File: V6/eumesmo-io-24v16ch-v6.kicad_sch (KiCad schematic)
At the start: 9 parts, among them J1 250-208, J2 250-208, J3 250-208, J4 250-208, J5 250-202

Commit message: Renamed all files to eumesmo branding
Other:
- sheet I2C Devices: file esp-24v-16ch-v6-i2c.kicad_sch -> eumesmo-io-24v16ch-v6-i2c.kicad_sch
- sheet Input 1: file esp-24v-16ch-v6-inputs1-8.kicad_sch -> eumesmo-io-24v16ch-v6-inputs1-8.kicad_sch
- sheet Input 10: file esp-24v-16ch-v6-inputs9-16.kicad_sch -> eumesmo-io-24v16ch-v6-inputs9-16.kicad_sch
- sheet Input 11: file esp-24v-16ch-v6-inputs9-16.kicad_sch -> eumesmo-io-24v16ch-v6-inputs9-16.kicad_sch
- sheet Input 12: file esp-24v-16ch-v6-inputs9-16.kicad_sch -> eumesmo-io-24v16ch-v6-inputs9-16.kicad_sch
- sheet Input 13: file esp-24v-16ch-v6-inputs9-16.kicad_sch -> eumesmo-io-24v16ch-v6-inputs9-16.kicad_sch
- sheet Input 14: file esp-24v-16ch-v6-inputs9-16.kicad_sch -> eumesmo-io-24v16ch-v6-inputs9-16.kicad_sch
- sheet Input 15: file esp-24v-16ch-v6-inputs9-16.kicad_sch -> eumesmo-io-24v16ch-v6-inputs9-16.kicad_sch
- sheet Input 16: file esp-24v-16ch-v6-inputs9-16.kicad_sch -> eumesmo-io-24v16ch-v6-inputs9-16.kicad_sch
- sheet Input 2: file esp-24v-16ch-v6-inputs1-8.kicad_sch -> eumesmo-io-24v16ch-v6-inputs1-8.kicad_sch
- sheet Input 3: file esp-24v-16ch-v6-inputs1-8.kicad_sch -> eumesmo-io-24v16ch-v6-inputs1-8.kicad_sch
- sheet Input 4: file esp-24v-16ch-v6-inputs1-8.kicad_sch -> eumesmo-io-24v16ch-v6-inputs1-8.kicad_sch
- sheet Input 5: file esp-24v-16ch-v6-inputs1-8.kicad_sch -> eumesmo-io-24v16ch-v6-inputs1-8.kicad_sch
- sheet Input 6: file esp-24v-16ch-v6-inputs1-8.kicad_sch -> eumesmo-io-24v16ch-v6-inputs1-8.kicad_sch
- sheet Input 7: file esp-24v-16ch-v6-inputs1-8.kicad_sch -> eumesmo-io-24v16ch-v6-inputs1-8.kicad_sch
- sheet Input 8: file esp-24v-16ch-v6-inputs1-8.kicad_sch -> eumesmo-io-24v16ch-v6-inputs1-8.kicad_sch
- sheet Input 9: file esp-24v-16ch-v6-inputs9-16.kicad_sch -> eumesmo-io-24v16ch-v6-inputs9-16.kicad_sch
- sheet LAN: file esp-24v-16ch-v6-lan.kicad_sch -> eumesmo-io-24v16ch-v6-lan.kicad_sch
- sheet MCU: file esp-24v-16ch-v6-mcu.kicad_sch -> eumesmo-io-24v16ch-v6-mcu.kicad_sch
- sheet Output 1: file esp-24v-16ch-v6-outputs1-8.kicad_sch -> eumesmo-io-24v16ch-v6-outputs1-8.kicad_sch
- sheet Output 10: file esp-24v-16ch-v6-outputs9-16.kicad_sch -> eumesmo-io-24v16ch-v6-outputs9-16.kicad_sch
- sheet Output 11: file esp-24v-16ch-v6-outputs9-16.kicad_sch -> eumesmo-io-24v16ch-v6-outputs9-16.kicad_sch
- sheet Output 12: file esp-24v-16ch-v6-outputs9-16.kicad_sch -> eumesmo-io-24v16ch-v6-outputs9-16.kicad_sch
- sheet Output 13: file esp-24v-16ch-v6-outputs9-16.kicad_sch -> eumesmo-io-24v16ch-v6-outputs9-16.kicad_sch
- sheet Output 14: file esp-24v-16ch-v6-outputs9-16.kicad_sch -> eumesmo-io-24v16ch-v6-outputs9-16.kicad_sch
- sheet Output 15: file esp-24v-16ch-v6-outputs9-16.kicad_sch -> eumesmo-io-24v16ch-v6-outputs9-16.kicad_sch
- sheet Output 16: file esp-24v-16ch-v6-outputs9-16.kicad_sch -> eumesmo-io-24v16ch-v6-outputs9-16.kicad_sch
- sheet Output 2: file esp-24v-16ch-v6-outputs1-8.kicad_sch -> eumesmo-io-24v16ch-v6-outputs1-8.kicad_sch
- sheet Output 3: file esp-24v-16ch-v6-outputs1-8.kicad_sch -> eumesmo-io-24v16ch-v6-outputs1-8.kicad_sch
- sheet Output 4: file esp-24v-16ch-v6-outputs1-8.kicad_sch -> eumesmo-io-24v16ch-v6-outputs1-8.kicad_sch
- sheet Output 5: file esp-24v-16ch-v6-outputs1-8.kicad_sch -> eumesmo-io-24v16ch-v6-outputs1-8.kicad_sch
- sheet Output 6: file esp-24v-16ch-v6-outputs1-8.kicad_sch -> eumesmo-io-24v16ch-v6-outputs1-8.kicad_sch
- sheet Output 7: file esp-24v-16ch-v6-outputs1-8.kicad_sch -> eumesmo-io-24v16ch-v6-outputs1-8.kicad_sch
- sheet Output 8: file esp-24v-16ch-v6-outputs1-8.kicad_sch -> eumesmo-io-24v16ch-v6-outputs1-8.kicad_sch
- sheet Output 9: file esp-24v-16ch-v6-outputs9-16.kicad_sch -> eumesmo-io-24v16ch-v6-outputs9-16.kicad_sch
- sheet Power: file esp-24v-16ch-v6-power.kicad_sch -> eumesmo-io-24v16ch-v6-power.kicad_sch
- title: ESP 24V 16xIn/16xOut/1-Wire Module -> eumesmo 24V 16xIn/16xOut/1-Wire Module

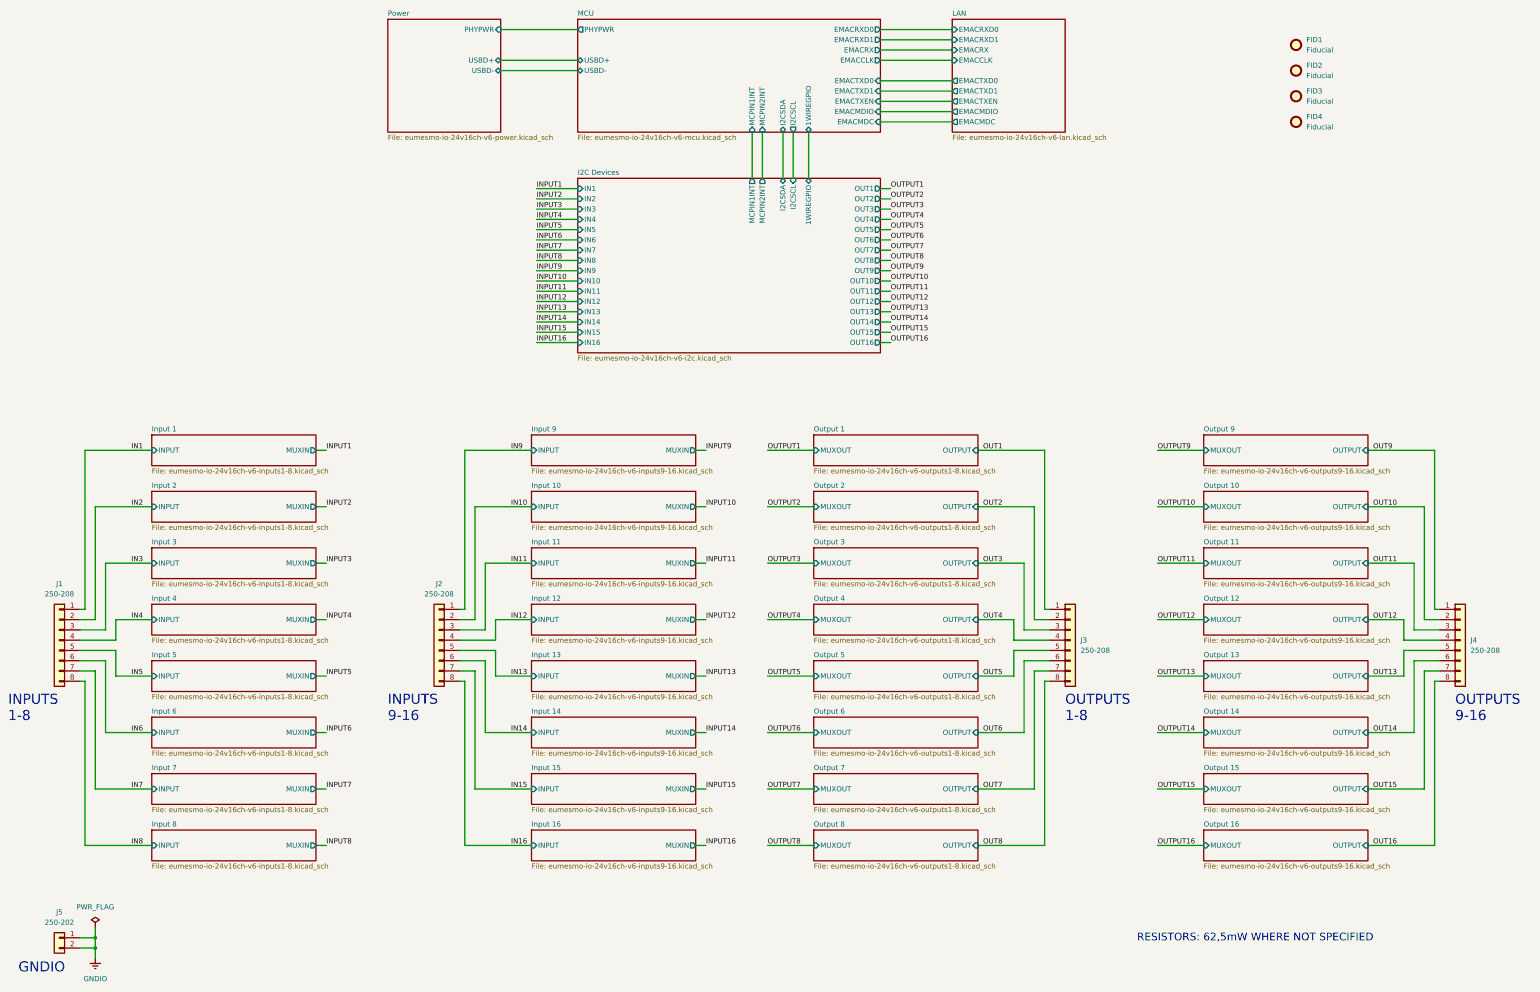
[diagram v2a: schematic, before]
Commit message: Added CPU health LED
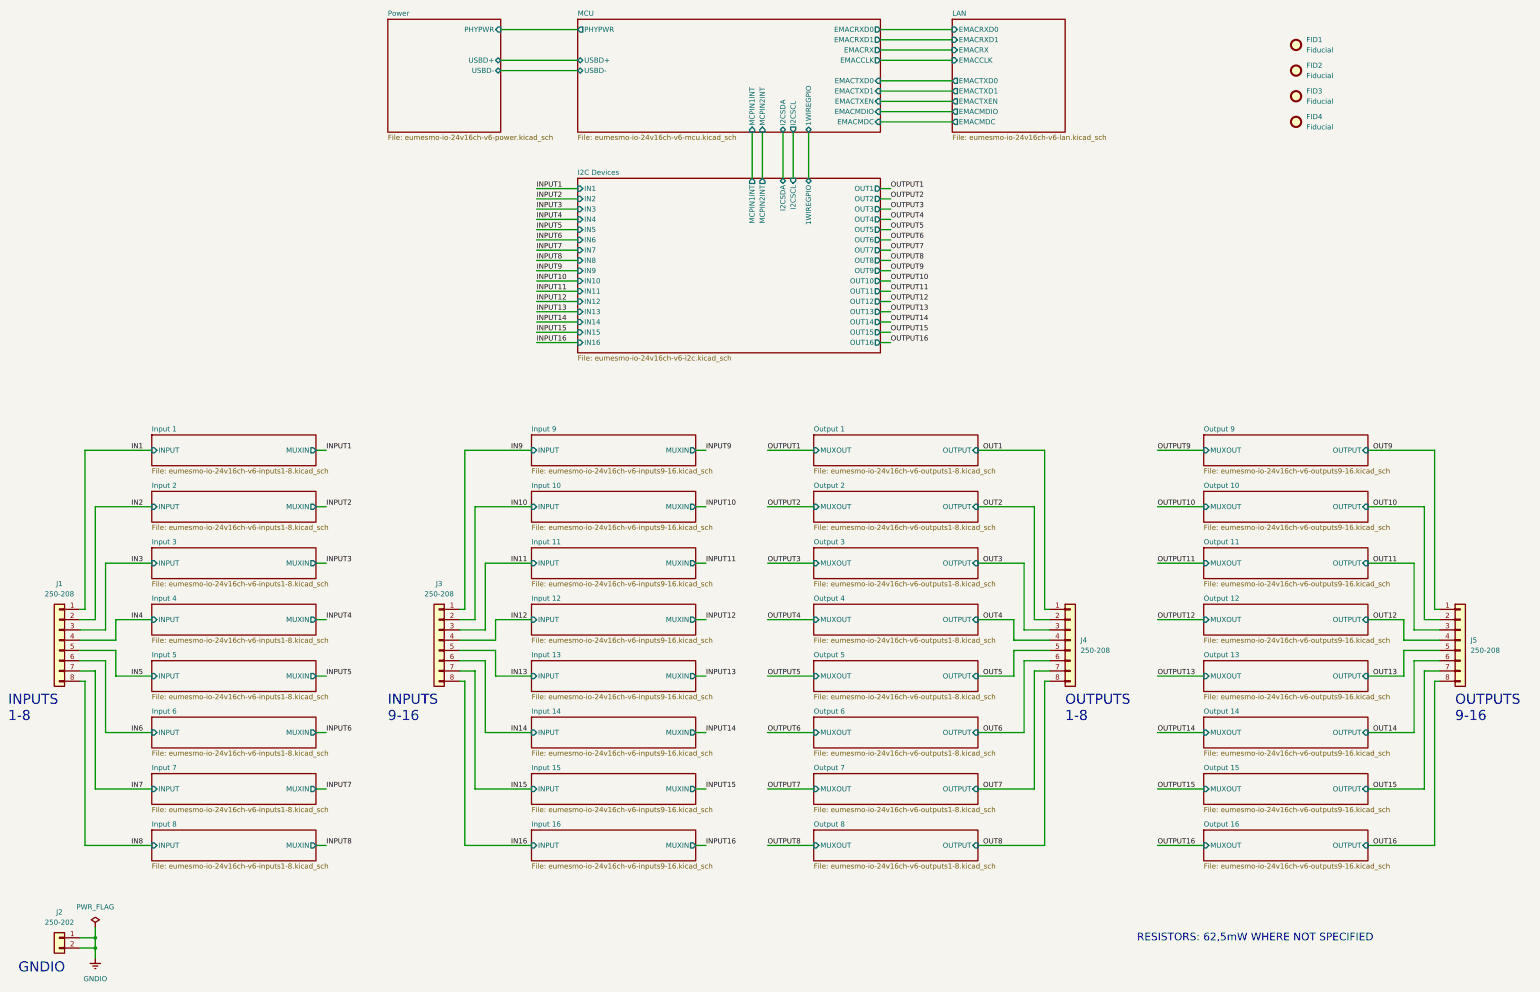
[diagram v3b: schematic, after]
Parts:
- renumbered J5 to J2, J2 to J3, J3 to J4, J4 to J5
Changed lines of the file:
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@@
 		(dnp no)
 		(fields_autoplaced yes)
-		(property "Reference" "J4"
+		(property "Reference" "J5"
 			(at 386.08 185.4199 0)
 			(show_name no)
@@
 			(project "eumesmo-io-24v16ch-v6"
 				(path "/2bc5a21a-1d79-419d-a592-6852cc07b00a"
-					(reference "J4")
+					(reference "J5")
 					(unit 1)
 				)
@@
 		(dnp no)
 		(fields_autoplaced yes)
-		(property "Reference" "J3"
+		(property "Reference" "J4"
 			(at 289.56 185.4199 0)
 			(show_name no)
@@
 			(project "eumesmo-io-24v16ch-v6"
 				(path "/2bc5a21a-1d79-419d-a592-6852cc07b00a"
-					(reference "J3")
+					(reference "J4")
 					(unit 1)
 				)
@@
 		(dnp no)
 		(fields_autoplaced yes)
-		(property "Reference" "J2"
+		(property "Reference" "J3"
 			(at 130.81 171.45 0)
 			(show_name no)
@@
 			(project "eumesmo-io-24v16ch-v6"
 				(path "/2bc5a21a-1d79-419d-a592-6852cc07b00a"
-					(reference "J2")
+					(reference "J3")
 					(unit 1)
 				)
@@
 		(dnp no)
 		(fields_autoplaced yes)
-		(property "Reference" "J5"
+		(property "Reference" "J2"
 			(at 36.83 252.73 0)
 			(show_name no)
@@
 			(project "eumesmo-io-24v16ch-v6"
 				(path "/2bc5a21a-1d79-419d-a592-6852cc07b00a"
-					(reference "J5")
+					(reference "J2")
 					(unit 1)
 				)
